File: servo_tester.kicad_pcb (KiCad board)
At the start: 2 copper layers, 50 x 100 mm, 35 parts, among them CON1 AVR-ISP-6, IC1 ATTINY2313-S, P1 CONN_01X02, P2 CONN_01X02, P3 CONN_01X03, P4 CONN_01X05, Q1 BC847, Q2 BC847, Q3 BC847, Q4 BC847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

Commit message: save before forward annotate test
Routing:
- net /mode_switch: track 106.7 -> 102.6 mm
- net GND: track 56.0 -> 53.0 mm, vias 8 -> 5
- net Net-(Q2-Pad1): track 9.03 -> 7.56 mm
- net /b: track 37.7 -> 36.9 mm
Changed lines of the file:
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@@
     (thickness 1.6)
     (drawings 4)
-    (tracks 270)
+    (tracks 268)
     (zones 0)
     (modules 35)
@@
   (via (at 171 85.5) (size 0.6) (drill 0.4) (layers F.Cu B.Cu) (net 10))
   (segment (start 171.055 85.555) (end 171 85.5) (width 0.5) (layer F.Cu) (net 10))
-  (segment (start 175.3 86.825) (end 172.325 86.825) (width 0.5) (layer F.Cu) (net 11))
+  (segment (start 173 87.75) (end 173 86.75) (width 0.5) (layer B.Cu) (net 11))
+  (segment (start 173.075 86.825) (end 175.3 86.825) (width 0.5) (layer F.Cu) (net 11) (status 800000))
+  (segment (start 173 86.75) (end 173.075 86.825) (width 0.5) (layer F.Cu) (net 11))
+  (via (at 173 86.75) (size 0.6) (drill 0.4) (layers F.Cu B.Cu) (net 11))
   (segment (start 181.2 110.55) (end 181.2 112.76) (width 0.5) (layer B.Cu) (net 11))
   (segment (start 181.25 110.5) (end 181.2 110.55) (width 0.5) (layer B.Cu) (net 11))
   (segment (start 173 110.5) (end 181.25 110.5) (width 0.5) (layer B.Cu) (net 11))
-  (segment (start 173 87.5) (end 173 110.5) (width 0.5) (layer B.Cu) (net 11))
-  (segment (start 172.25 86.75) (end 173 87.5) (width 0.5) (layer B.Cu) (net 11))
-  (via (at 172.25 86.75) (size 0.6) (drill 0.4) (layers F.Cu B.Cu) (net 11))
-  (segment (start 172.325 86.825) (end 172.25 86.75) (width 0.5) (layer F.Cu) (net 11))
+  (segment (start 173 87.5) (end 173 87.75) (width 0.5) (layer B.Cu) (net 11))
+  (segment (start 173 87.75) (end 173 110.5) (width 0.5) (layer B.Cu) (net 11))
   (segment (start 175.3 94.445) (end 176.695 94.445) (width 0.5) (layer F.Cu) (net 12))
   (segment (start 173.58 106.67) (end 173.58 112.76) (width 0.5) (layer F.Cu) (net 12))
@@
   (segment (start 177.5 95.25) (end 177.5 102.75) (width 0.5) (layer F.Cu) (net 12))
   (segment (start 176.695 94.445) (end 177.5 95.25) (width 0.5) (layer F.Cu) (net 12))
+  (segment (start 171.75 137.025) (end 167.225 132.5) (width 0.5) (layer F.Cu) (net 13))
+  (segment (start 167.225 132.5) (end 165 132.5) (width 0.5) (layer F.Cu) (net 13))
   (segment (start 174.75 98.5) (end 172.25 96) (width 0.5) (layer F.Cu) (net 13))
-  (via (at 174.75 98.5) (size 0.6) (drill 0.4) (layers F.Cu B.Cu) (net 13))
-  (segment (start 167.55 97.45) (end 167.55 98.99886) (width 0.5) (layer F.Cu) (net 13) (status 800000))
+  (segment (start 167.55 97.45) (end 167.55 98.99886) (width 0.5) (layer F.Cu) (net 13))
   (segment (start 169 96) (end 167.55 97.45) (width 0.5) (layer F.Cu) (net 13))
   (segment (start 172.25 96) (end 169 96) (width 0.5) (layer F.Cu) (net 13))
@@
   (segment (start 174.75 98.5) (end 174.75 100) (width 0.5) (layer F.Cu) (net 13))
   (via (at 176.5 102.25) (size 0.6) (drill 0.4) (layers F.Cu B.Cu) (net 13))
-  (segment (start 174.75 96.25) (end 175 96) (width 0.5) (layer F.Cu) (net 13) (status 800000))
-  (segment (start 175 96) (end 175.3 95.715) (width 0.5) (layer F.Cu) (net 13) (status C00000))
-  (via (at 189 108.75) (size 0.6) (drill 0.4) (layers F.Cu B.Cu) (net 13))
-  (via (at 186 108.75) (size 0.6) (drill 0.4) (layers F.Cu B.Cu) (net 13))
-  (segment (start 189 108.75) (end 186 108.75) (width 0.5) (layer F.Cu) (net 13))
+  (segment (start 174.75 96.25) (end 175 96) (width 0.5) (layer F.Cu) (net 13))
+  (segment (start 175 96) (end 175.3 95.715) (width 0.5) (layer F.Cu) (net 13))
   (segment (start 189.45 141.25114) (end 191.24886 141.25114) (width 0.5) (layer F.Cu) (net 13))
   (segment (start 191.25 141.25) (end 191.5 141.25) (width 0.5) (layer B.Cu) (net 13))
@@
   (via (at 182 139.5) (size 0.6) (drill 0.4) (layers F.Cu B.Cu) (net 13))
   (segment (start 181.45 140.05) (end 182 139.5) (width 0.5) (layer F.Cu) (net 13))
-  (segment (start 165 132.5) (end 167.225 132.5) (width 0.5) (layer F.Cu) (net 13))
-  (segment (start 167.225 132.5) (end 171.75 137.025) (width 0.5) (layer F.Cu) (net 13))
   (segment (start 180.77 66) (end 180.77 65.73) (width 0.5) (layer F.Cu) (net 13))
   (via (at 180.77 65.73) (size 0.6) (drill 0.4) (layers F.Cu B.Cu) (net 13))
@@
   (segment (start 169.1 73.15) (end 169 73.25) (width 0.5) (layer F.Cu) (net 16))
   (segment (start 173 69.35) (end 173 73.15) (width 0.5) (layer F.Cu) (net 16))
-  (segment (start 184 138.15) (end 184 98) (width 0.5) (layer F.Cu) (net 17))
-  (segment (start 182.675 86.825) (end 184.7 86.825) (width 0.5) (layer F.Cu) (net 17))
+  (segment (start 182.5 89.5) (end 182.5 95) (width 0.5) (layer B.Cu) (net 17))
+  (via (at 182.5 89.5) (size 0.6) (drill 0.4) (layers F.Cu B.Cu) (net 17))
+  (segment (start 182.5 89.5) (end 182.5 87) (width 0.5) (layer F.Cu) (net 17))
   (segment (start 182.5 87) (end 182.675 86.825) (width 0.5) (layer F.Cu) (net 17))
-  (segment (start 182.5 89.5) (end 182.5 87) (width 0.5) (layer F.Cu) (net 17))
-  (via (at 182.5 89.5) (size 0.6) (drill 0.4) (layers F.Cu B.Cu) (net 17))
-  (segment (start 182.5 96.5) (end 182.5 89.5) (width 0.5) (layer B.Cu) (net 17))
-  (segment (start 184 98) (end 182.5 96.5) (width 0.5) (layer B.Cu) (net 17))
-  (via (at 184 98) (size 0.6) (drill 0.4) (layers F.Cu B.Cu) (net 17))
+  (segment (start 184.7 86.825) (end 182.675 86.825) (width 0.5) (layer F.Cu) (net 17))
+  (segment (start 184 99) (end 184 138.15) (width 0.5) (layer F.Cu) (net 17))
+  (segment (start 182.5 97.5) (end 184 99) (width 0.5) (layer F.Cu) (net 17))
+  (segment (start 182.5 95) (end 182.5 97.5) (width 0.5) (layer F.Cu) (net 17))
+  (via (at 182.5 95) (size 0.6) (drill 0.4) (layers F.Cu B.Cu) (net 17))
   (segment (start 194 83) (end 191 83) (width 0.5) (layer B.Cu) (net 17))
   (segment (start 187.175 86.825) (end 184.7 86.825) (width 0.5) (layer F.Cu) (net 17))
@@
   (segment (start 181 136.25) (end 181 134.35) (width 0.5) (layer F.Cu) (net 28))
   (segment (start 180.5 136.75) (end 181 136.25) (width 0.5) (layer F.Cu) (net 28))
-  (segment (start 181.7 102.99886) (end 181.7 101.05) (width 0.5) (layer F.Cu) (net 29))
-  (segment (start 185.4 102.85) (end 187.25 102.85) (width 0.5) (layer F.Cu) (net 29))
-  (segment (start 185.25 103) (end 185.4 102.85) (width 0.5) (layer F.Cu) (net 29))
-  (via (at 185.25 103) (size 0.6) (drill 0.4) (layers F.Cu B.Cu) (net 29))
-  (segment (start 182.5 100.25) (end 185.25 103) (width 0.5) (layer B.Cu) (net 29))
-  (via (at 182.5 100.25) (size 0.6) (drill 0.4) (layers F.Cu B.Cu) (net 29))
-  (segment (start 181.7 101.05) (end 182.5 100.25) (width 0.5) (layer F.Cu) (net 29))
+  (segment (start 181.7 102.99886) (end 181.7 103.7) (width 0.5) (layer F.Cu) (net 29))
+  (segment (start 181.7 103.7) (end 182.75 104.75) (width 0.5) (layer F.Cu) (net 29))
+  (via (at 182.75 104.75) (size 0.6) (drill 0.4) (layers F.Cu B.Cu) (net 29))
+  (segment (start 182.75 104.75) (end 185.5 104.75) (width 0.5) (layer B.Cu) (net 29))
+  (via (at 185.5 104.75) (size 0.6) (drill 0.4) (layers F.Cu B.Cu) (net 29))
+  (segment (start 185.5 104.75) (end 187.25 103) (width 0.5) (layer F.Cu) (net 29))
+  (segment (start 187.25 103) (end 187.25 102.85) (width 0.5) (layer F.Cu) (net 29))
   (segment (start 180.75 106.00114) (end 178.89886 106.00114) (width 0.5) (layer F.Cu) (net 30))
   (segment (start 178.89886 106.00114) (end 178.75 106.15) (width 0.5) (layer F.Cu) (net 30))
@@
   (segment (start 178.5 93) (end 178.675 93.175) (width 0.25) (layer F.Cu) (net 37))
   (segment (start 178.675 93.175) (end 184.7 93.175) (width 0.25) (layer F.Cu) (net 37))
-  (segment (start 176.25 137.025) (end 176.25 136.75) (width 0.25) (layer F.Cu) (net 38))
-  (segment (start 176.25 136.75) (end 170 130.5) (width 0.25) (layer F.Cu) (net 38))
+  (segment (start 166 82) (end 167.5 83.5) (width 0.25) (layer F.Cu) (net 38))
   (segment (start 170 130.5) (end 162.5 130.5) (width 0.25) (layer F.Cu) (net 38))
   (segment (start 162.5 130.5) (end 156 124) (width 0.25) (layer F.Cu) (net 38))
@@
   (segment (start 158.5 80) (end 164 80) (width 0.25) (layer F.Cu) (net 38))
   (segment (start 164 80) (end 166 82) (width 0.25) (layer F.Cu) (net 38))
-  (segment (start 166 82) (end 177 82) (width 0.25) (layer F.Cu) (net 38))
-  (via (at 177 82) (size 0.6) (drill 0.4) (layers F.Cu B.Cu) (net 38))
-  (segment (start 177 82) (end 176 83) (width 0.25) (layer B.Cu) (net 38))
-  (segment (start 176 83) (end 176 87.5) (width 0.25) (layer B.Cu) (net 38))
-  (segment (start 176 87.5) (end 180.5 92) (width 0.25) (layer B.Cu) (net 38))
-  (via (at 180.5 92) (size 0.6) (drill 0.4) (layers F.Cu B.Cu) (net 38))
-  (segment (start 180.5 92) (end 180.595 91.905) (width 0.25) (layer F.Cu) (net 38))
-  (segment (start 180.595 91.905) (end 184.7 91.905) (width 0.25) (layer F.Cu) (net 38))
+  (segment (start 176.25 136.75) (end 170 130.5) (width 0.25) (layer F.Cu) (net 38))
+  (segment (start 180.095 91.905) (end 184.7 91.905) (width 0.25) (layer F.Cu) (net 38) (status 800000))
+  (segment (start 180 92) (end 180.095 91.905) (width 0.25) (layer F.Cu) (net 38))
+  (via (at 180 92) (size 0.6) (drill 0.4) (layers F.Cu B.Cu) (net 38))
+  (segment (start 180 91) (end 180 92) (width 0.25) (layer B.Cu) (net 38))
+  (segment (start 172.5 83.5) (end 180 91) (width 0.25) (layer B.Cu) (net 38))
+  (via (at 172.5 83.5) (size 0.6) (drill 0.4) (layers F.Cu B.Cu) (net 38))
+  (segment (start 167.5 83.5) (end 172.5 83.5) (width 0.25) (layer F.Cu) (net 38))
+  (segment (start 176.25 137.025) (end 176.25 136.75) (width 0.25) (layer F.Cu) (net 38))
   (segment (start 175.3 89.365) (end 167.48386 89.365) (width 0.5) (layer F.Cu) (net 39))
   (segment (start 167.48386 89.365) (end 163 93.84886) (width 0.5) (layer F.Cu) (net 39))

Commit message: starting with drc now
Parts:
- added C4: 100nF, Capacitors_SMD:C_0805_HandSoldering, F.Cu at (184.8, 80.8)
- added D3: LED, LEDs:LED_0805, F.Cu at (197.2, 134.5)
- added R11: 1k, Resistors_SMD:R_0805_HandSoldering, F.Cu at (197.2, 139.5)
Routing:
- net +5V: track 130.4 -> 183.9 mm
- net /mode_switch: track 102.6 -> 112.2 mm
- net Net-(D3-Pad2): track 0.00 -> 2.60 mm
- net GND: track 53.0 -> 52.2 mm, vias 5 -> 8

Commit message: oops... attiny2313 doesnt have adc...
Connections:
- P4 pad 2: Net-(P4-Pad2) -> /pot_in
- P4 pad 3: Net-(P4-Pad3) -> /mode_switch
- P4 pad 4: Net-(P4-Pad4) -> /pwm_out
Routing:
- net /mode_switch: track 112.2 -> 167.9 mm
- net /pot_in: track 99.3 -> 118.9 mm, vias 0 -> 3
- net +5V: track 183.9 -> 192.0 mm, vias 0 -> 1
- net /pwm_out: track 20.2 -> 27.3 mm

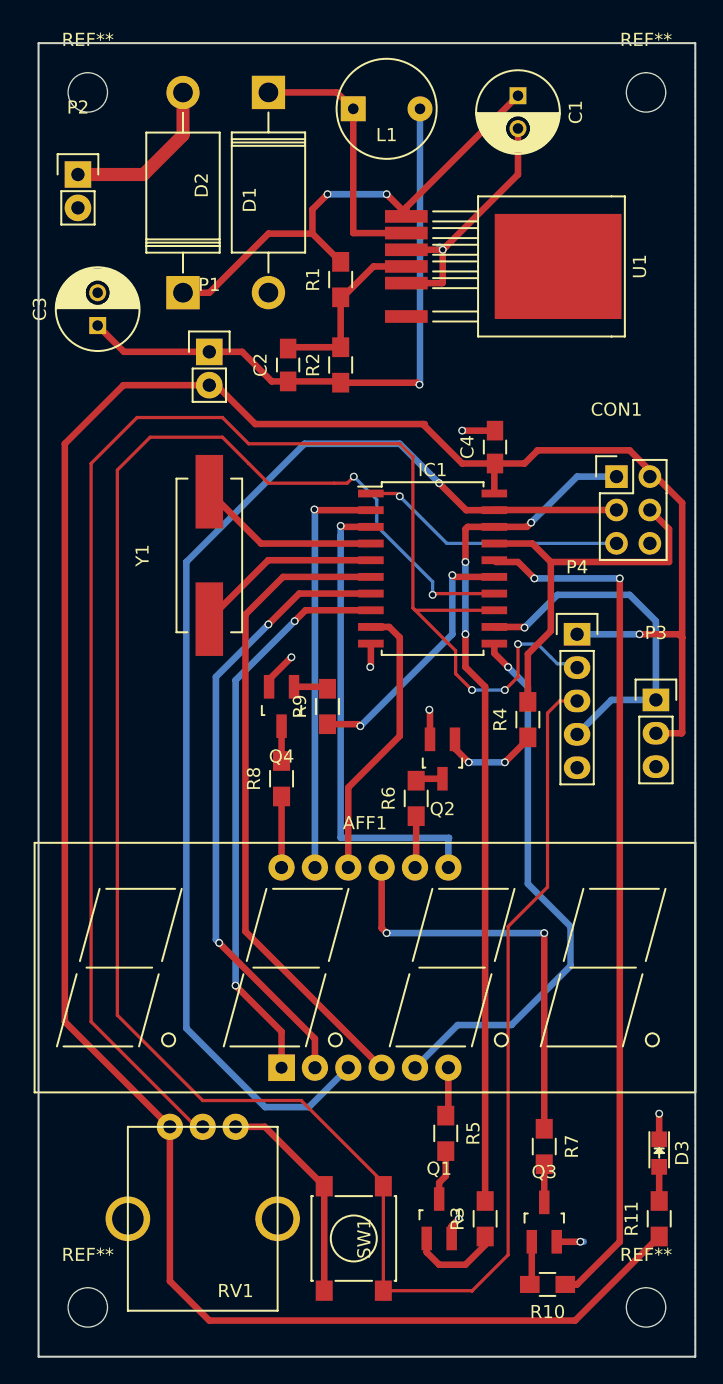
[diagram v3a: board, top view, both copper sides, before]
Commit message: adjusted - adc now via AVR400 application note
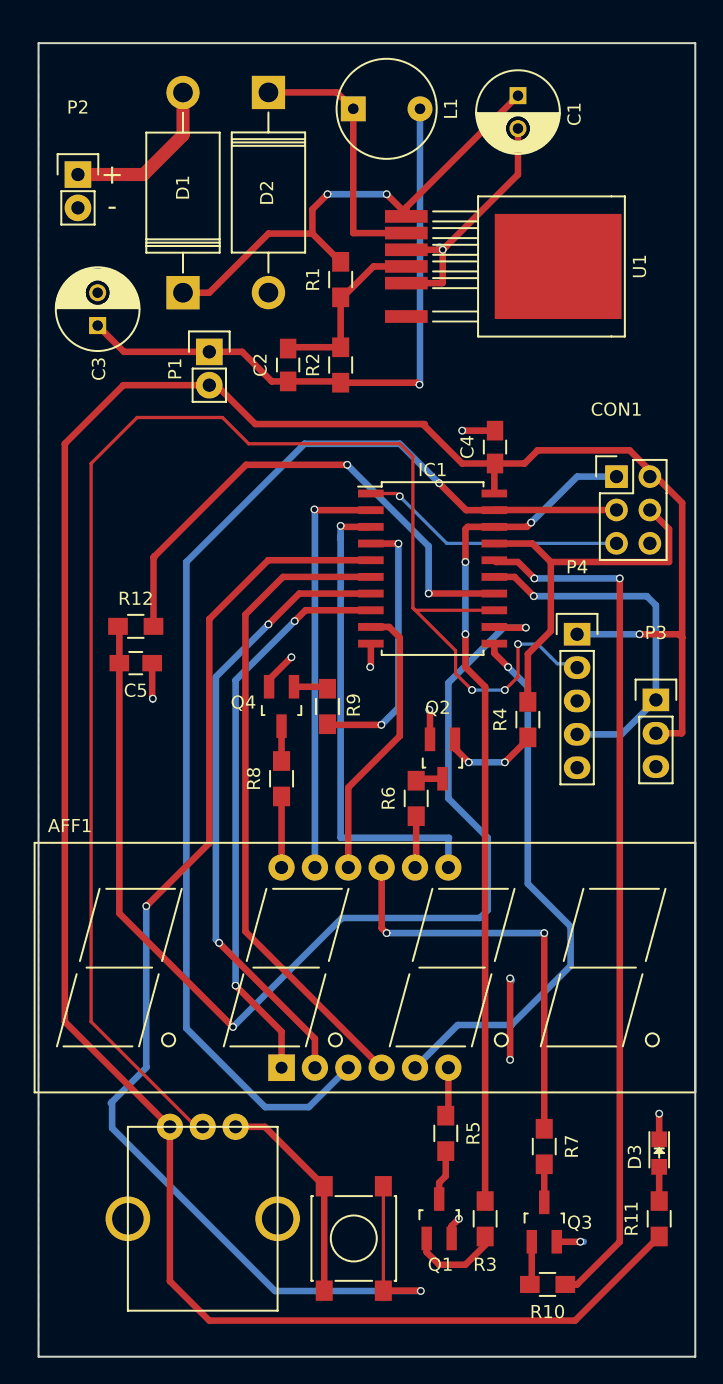
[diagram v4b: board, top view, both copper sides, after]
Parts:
- removed REF** (x4): MountingHole_3mm, Mounting_Holes:MountingHole_3mm
- removed Y1: Crystal, Crystals:Crystal_HC49-SD_SMD
- added C5: 4.7nF, Capacitors_SMD:C_0805_HandSoldering, F.Cu at (157.4, 97.2)
- added R12: 27k, Resistors_SMD:R_0805_HandSoldering, F.Cu at (157.4, 94.4)
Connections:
- IC1 pad 12: /pwm_out -> Net-(C5-Pad2)
- IC1 pad 14: /mode_switch -> Net-(IC1-Pad14)
- IC1 pad 15: /c1 -> /pwm_out
- IC1 pad 4: Net-(IC1-Pad4) -> /c1
- SW1 pad 1: /mode_switch -> Net-(IC1-Pad5)
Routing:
- net /mode_switch: track 167.9 -> 0.00 mm, vias 2 -> 0
- net Net-(C5-Pad2): track 0.00 -> 85.8 mm, vias 0 -> 2
- net Net-(IC1-Pad5): track 14.2 -> 95.8 mm, vias 0 -> 2
- net Net-(IC1-Pad14): track 0.00 -> 40.4 mm, vias 0 -> 2
- net Net-(IC1-Pad4): track 13.9 -> 0.00 mm
- net GND: track 52.2 -> 61.4 mm, vias 8 -> 11
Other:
- rule trace_min: 0.2 -> 0.1524
- board text added: "+"
- board text added: "-"

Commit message: final check again...
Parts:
- added REF**: MountingHole_3mm, Mounting_Holes:MountingHole_3mm, F.Cu at (196.2, 53.8)
- added REF**: MountingHole_3mm, Mounting_Holes:MountingHole_3mm, F.Cu at (153.8, 53.8)
- added REF**: MountingHole_3mm, Mounting_Holes:MountingHole_3mm, F.Cu at (153.8, 146.2)
- added REF**: MountingHole_3mm, Mounting_Holes:MountingHole_3mm, F.Cu at (196.2, 146.2)
- U1: footprint Power_Integrations:TO-263-7C -> smd-semi:TO-263-5
- moved U1 10.8 mm to (188.8, 67.1), turned to 0 degrees
- renumbered P4 to DBG, CON1 to ISP, P3 to SERVO
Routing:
- net (no net): track 0.00 -> 6.81 mm, vias 0 -> 2
- net GND: track 61.4 -> 56.4 mm, vias 11 -> 8
- net Net-(C2-Pad2): track 13.8 -> 17.8 mm
- net Net-(D2-Pad1): track 20.5 -> 23.0 mm
- net Net-(C1-Pad1): track 37.8 -> 39.7 mm

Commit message: Submitted to seeedstudio
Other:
- board text added: "servo_tester Tobias Kaiser Oct 10 2016"
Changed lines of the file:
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@@
     (links 77)
     (no_connects 1)
-    (area 149.924999 49.924999 200.075001 150.075001)
+    (area 147.111474 48.4745 204.890046 152.37626)
     (thickness 1.6)
-    (drawings 6)
+    (drawings 7)
     (tracks 332)
     (zones 0)
@@
   (page A4)
   (layers
-    (0 F.Cu signal)
-    (31 B.Cu signal)
+    (0 F.Cu signal hide)
+    (31 B.Cu signal hide)
     (32 B.Adhes user)
     (33 F.Adhes user)
@@
     (visible_elements FFFEFF7F)
     (pcbplotparams
-      (layerselection 0x00030_80000001)
+      (layerselection 0x010f0_80000001)
       (usegerberextensions false)
       (excludeedgelayer true)
@@
       (outputformat 1)
       (mirror false)
-      (drillshape 1)
+      (drillshape 0)
       (scaleselection 1)
-      (outputdirectory ""))
+      (outputdirectory gerber/))
   )
   (net 0 "")
@@
     (pad 1 thru_hole circle (at 0 0) (size 3 3) (drill 3) (layers))
   )
+  (gr_text "servo_tester\nTobias Kaiser\nOct 10 2016" (at 161.25 83.75) (layer F.SilkS)
+    (effects (font (size 1.5 1.5) (thickness 0.3)))
+  )
   (gr_text + (at 155.6 60) (layer F.SilkS)
